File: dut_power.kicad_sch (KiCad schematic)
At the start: 59 parts, among them J10 Conn_02x04_Odd_Even, J7 Conn_02x04_Odd_Even, J8 Conn_01x02, J9 Conn_02x04_Odd_Even, Q1 AO3401A, U1 TCA9535PWR(UMW)

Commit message: FIXUP load switch
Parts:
- removed D10, D12, D6, D8: RED, LED_SMD:LED_0603_1608Metric, symbol Device:LED
- removed D11, D5, D7, D9: GREEN, LED_SMD:LED_0603_1608Metric, symbol Device:LED
- removed R10, R12, R6, R8: 2k, Resistor_SMD:R_0603_1608Metric, symbol Device:R
- removed R11, R5, R7, R9: 1.5k, Resistor_SMD:R_0603_1608Metric, symbol Device:R
- added F1: Fuse, HL_Fuse:FUSE-TH_L22.6-W9.0, symbol Device:Fuse
- J8: footprint Connector_Phoenix_MC:PhoenixContact_MC_1,5_2-G-3.81_1x02_P3.81mm_Horizontal -> Connector_Phoenix_MC:PhoenixContact_MCV_1,5_2-G-3.81_1x02_P3.81mm_Vertical
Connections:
- net Vin: now also F1.2; no longer J8.2 (Pin_2)
- new net: F1.1, J8.2 (Pin_2)
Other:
- sheet Curlim 1 renamed Load switch 5V 1
- sheet Curlim 12V 1 renamed Load switch 12V 1
- sheet Curlim 12V 2 renamed Load switch 12V 2
- sheet Curlim 2 renamed Load switch 5V 2
- sheet Curlim 3 renamed Load switch 5V 3
- sheet Curlim 4 renamed Load switch 5V 4
- sheet Load switch 12V 1: file curlim_12V.kicad_sch -> load_switch_12V.kicad_sch
- sheet Load switch 12V 2: file curlim_12V.kicad_sch -> load_switch_12V.kicad_sch
- sheet Load switch 5V 1: file curlim_2.7-5.5V.kicad_sch -> load_switch_5v.kicad_sch
- sheet Load switch 5V 2: file curlim_2.7-5.5V.kicad_sch -> load_switch_5v.kicad_sch
- sheet Load switch 5V 3: file curlim_2.7-5.5V.kicad_sch -> load_switch_5v.kicad_sch
- sheet Load switch 5V 4: file curlim_2.7-5.5V.kicad_sch -> load_switch_5v.kicad_sch
- moved on the sheet: J8

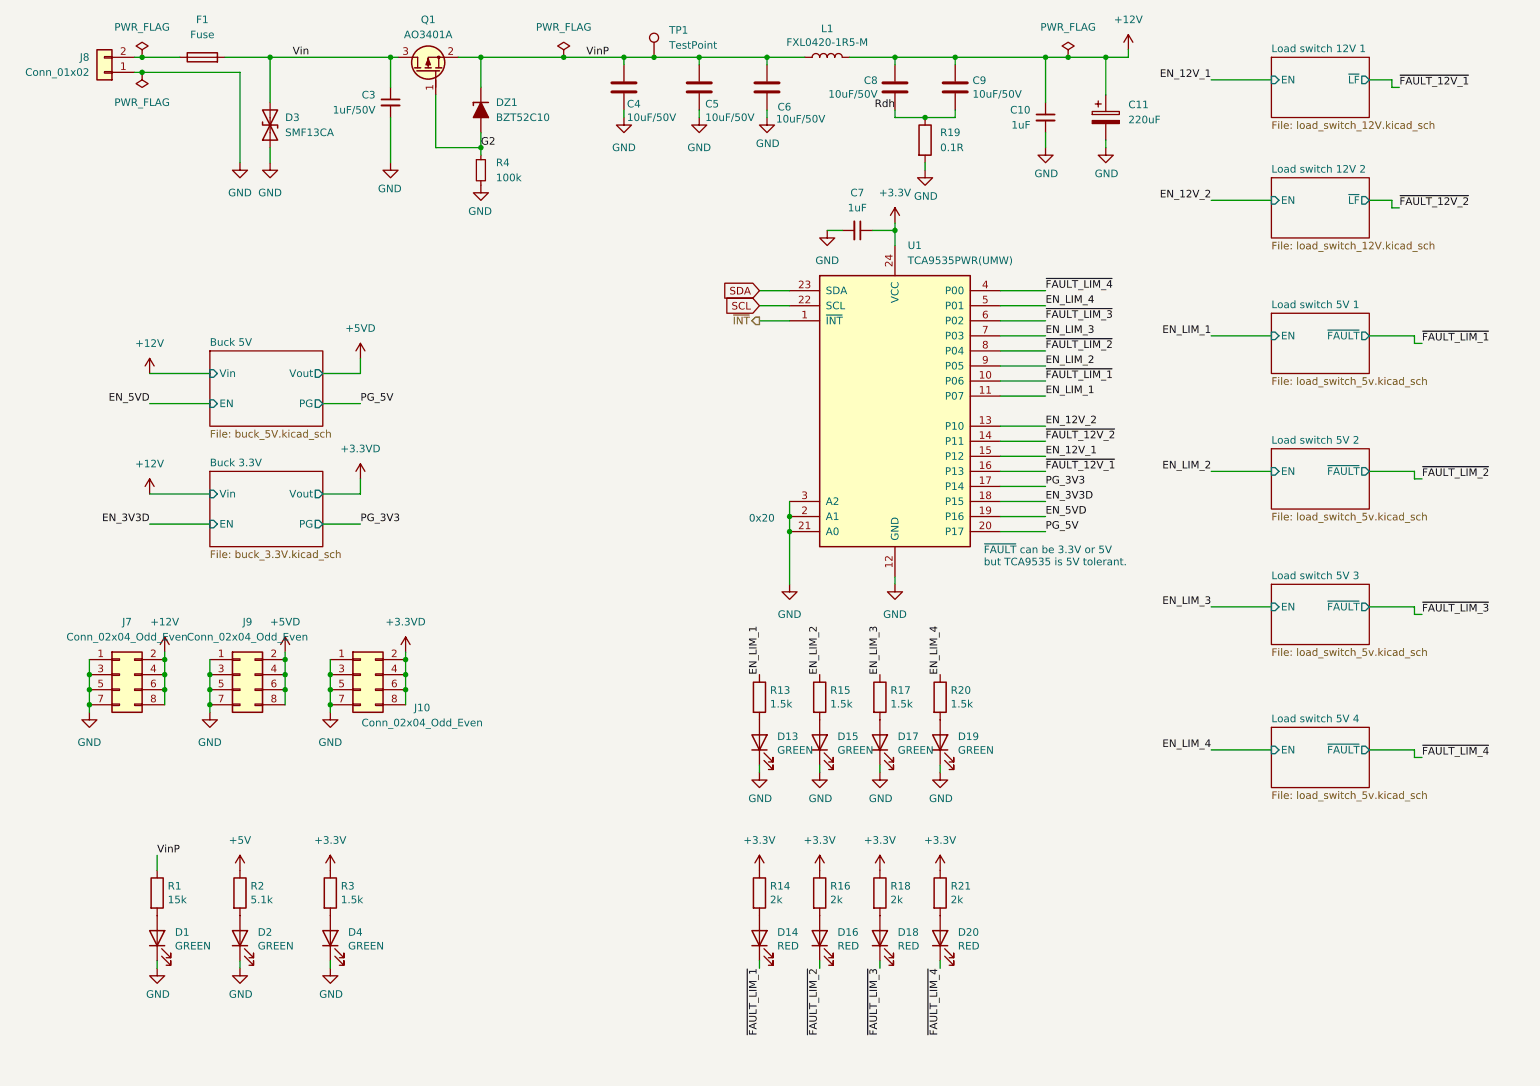
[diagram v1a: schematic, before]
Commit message: Update the design to a stackable one
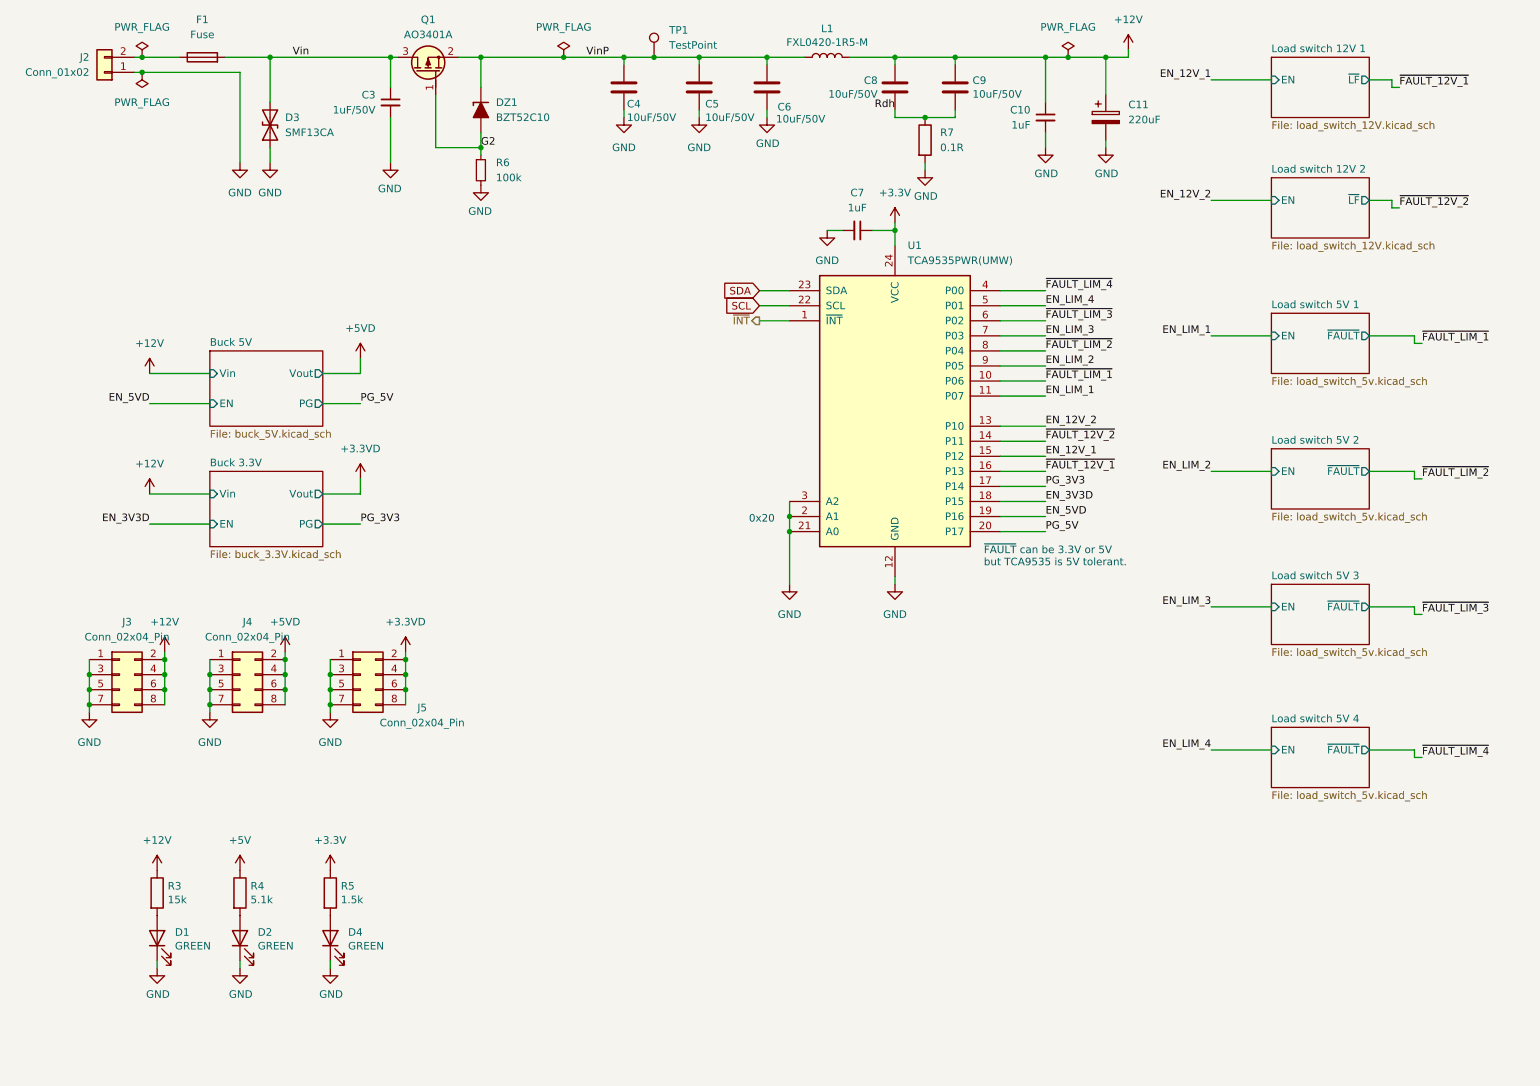
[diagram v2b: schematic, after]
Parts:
- removed D13, D15, D17, D19: GREEN, LED_SMD:LED_0603_1608Metric, symbol Device:LED
- removed D14, D16, D18, D20: RED, LED_SMD:LED_0603_1608Metric, symbol Device:LED
- removed R13, R15, R17, R20: 1.5k, Resistor_SMD:R_0603_1608Metric, symbol Device:R
- removed R14, R16, R18, R21: 2k, Resistor_SMD:R_0603_1608Metric, symbol Device:R
- F1: LCSC (none) -> C3131
- J2: renamed from J8; LCSC C8387 -> C8396
- J3: renamed from J7; value Conn_02x04_Odd_Even -> Conn_02x04_Pin; JLCPCB_CORRECTION 1.27;3.81;270 -> 1.27;-3.81;270
- J4: renamed from J9; value Conn_02x04_Odd_Even -> Conn_02x04_Pin; JLCPCB_CORRECTION 1.27;3.81;270 -> 1.27;-3.81;270
- J5: renamed from J10; value Conn_02x04_Odd_Even -> Conn_02x04_Pin; JLCPCB_CORRECTION 1.27;3.81;270 -> 1.27;-3.81;270
- renumbered R1 to R3, R2 to R4, R3 to R5, R4 to R6, R19 to R7
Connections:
- net +12V: now also R3.1
- net VinP: no longer R3.1
